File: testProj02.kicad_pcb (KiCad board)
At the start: 2 copper layers, 50 x 29 mm, 29 parts, among them J1 Conn_02x03_Odd_Even, J2 Conn_01x09_Pin, J3 Conn_01x04_Pin, J4 Conn_01x04_Pin, U1 24LC1025, U2 DS1337S_, U3 24LC1025, U4 ATMEGA328P-AU, Y1 32.768 KHZ, Y2 16 Mhz

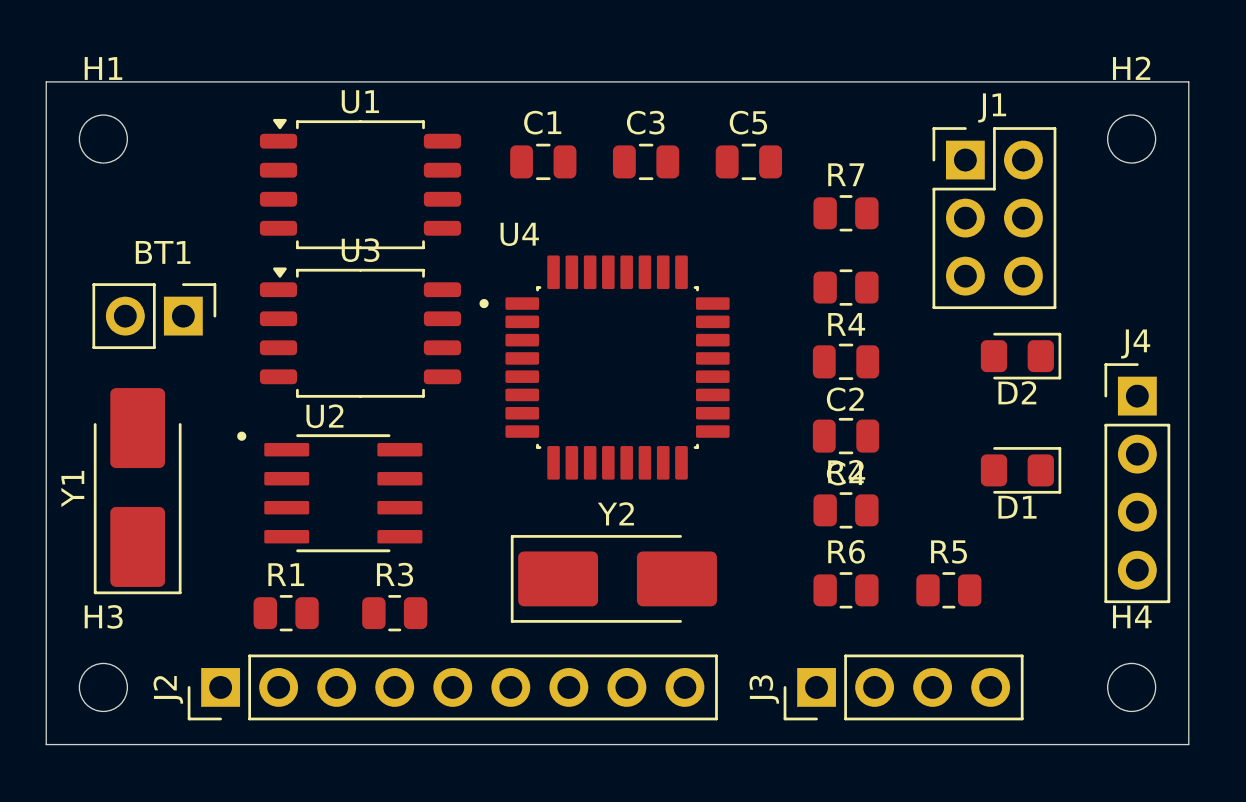
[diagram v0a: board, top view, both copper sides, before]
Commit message: layout arrange components
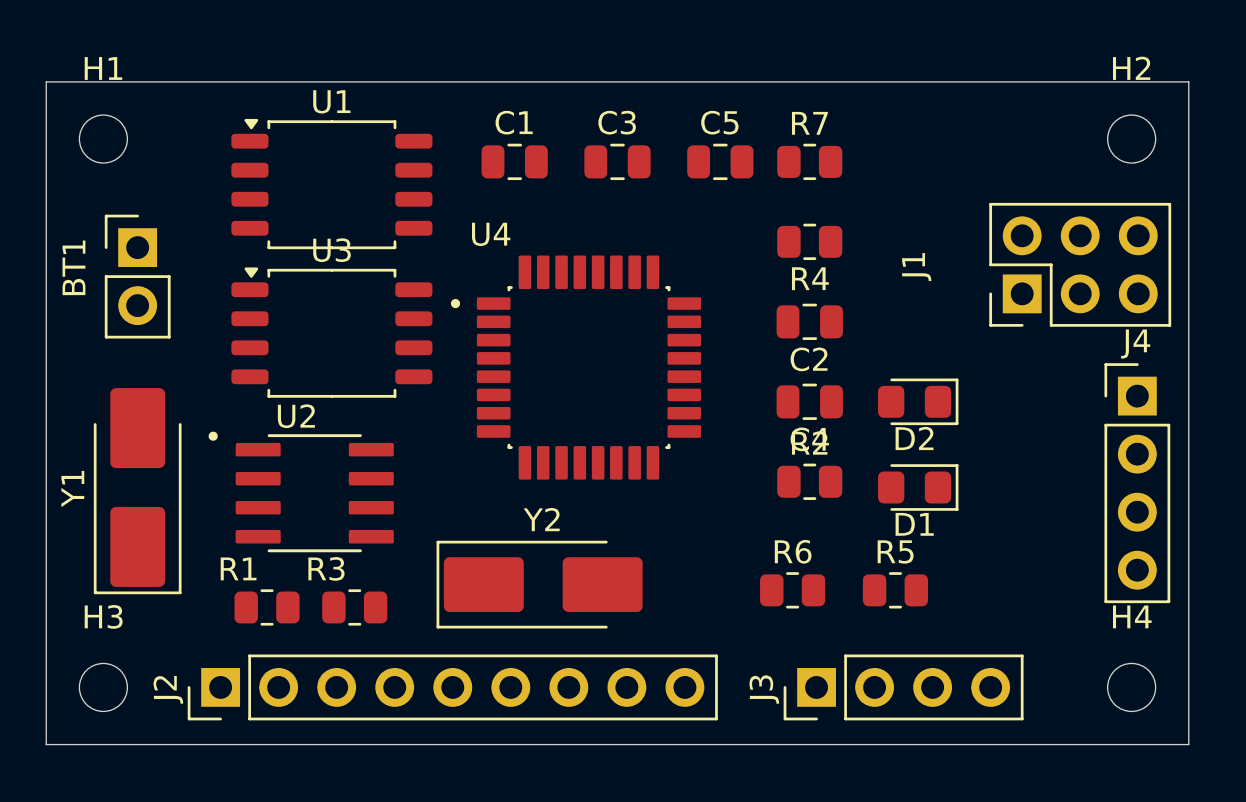
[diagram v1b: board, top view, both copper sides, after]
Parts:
- moved J1 6.36 mm to (104.7, 87.3), turned to 90 degrees
- moved D2 4.92 mm to (100.0, 92.0)
- moved D1 4.56 mm to (100.0, 95.8)
- moved BT1 3.61 mm to (66.0, 85.2), turned to 0 degrees
- moved Y2 3.26 mm to (83.8, 100.0)
- moved R7 2.75 mm to (95.4, 81.5)
- moved R4 2.55 mm to (95.4, 85.0)
- moved C2 2.36 mm to (95.4, 88.5)
- moved R5 2.34 mm to (99.2, 100.2)
- moved R6 2.34 mm to (94.7, 100.2)
- moved C4 2.18 mm to (95.4, 92.0)
- moved R2 2.02 mm to (95.4, 95.5)
- moved R3 1.77 mm to (75.5, 101.0)
- moved C1 1.25 mm to (82.5, 81.5)
- moved C3 1.25 mm to (87.0, 81.5)
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
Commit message: test
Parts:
- moved D1 4.73 mm to (104.7, 95.5)
- moved D2 4.73 mm to (104.7, 91.8)
- moved C1 1.80 mm to (84.0, 80.5)
- moved C3 1.80 mm to (88.5, 80.5)
- moved C5 1.80 mm to (93.0, 80.5)
- moved R7 1.80 mm to (96.9, 80.5)
- moved C2 1.68 mm to (97.1, 88.5)
- moved C4 1.68 mm to (97.1, 92.0)
- moved R2 1.68 mm to (97.1, 95.5)
- moved R4 1.68 mm to (97.1, 85.0)
- moved R5 1.68 mm to (100.8, 100.2)
- moved R6 1.68 mm to (96.3, 100.2)
- moved U4 1.50 mm to (87.2, 90.5)
- moved U1 1.03 mm to (74.8, 81.5)
- moved U3 0.25 mm to (74.8, 89.0)
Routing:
- net GND: track 0.00 -> 162.2 mm
- net /Vcc: track 0.00 -> 157.1 mm
- net /SCK: track 0.00 -> 86.0 mm, vias 0 -> 5
- net /SDA: track 0.00 -> 76.5 mm, vias 0 -> 2
- net Net-(BT1-+): track 0.00 -> 68.5 mm, vias 0 -> 2
- net /TX: track 0.00 -> 58.6 mm, vias 0 -> 2
- net /RX: track 0.00 -> 50.0 mm, vias 0 -> 1
- net /RESET: track 0.00 -> 49.9 mm, vias 0 -> 3
- net Net-(U4-PB6): track 0.00 -> 43.0 mm, vias 0 -> 2
- net Net-(U4-PB7): track 0.00 -> 41.0 mm, vias 0 -> 3
- net Net-(D2-K): track 0.00 -> 36.2 mm
- net /D2: track 0.00 -> 34.0 mm, vias 0 -> 1
- net /MOSI: track 0.00 -> 32.0 mm, vias 0 -> 2
- net /D3: track 0.00 -> 27.3 mm, vias 0 -> 1
- net /D4: track 0.00 -> 23.9 mm, vias 0 -> 3
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- added copper zone on B.Cu, net GND
- added copper zone on F.Cu, net GND
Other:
- board size 50 x 29 mm -> 50.5 x 30 mm
